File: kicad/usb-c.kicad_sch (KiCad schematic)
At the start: 12 parts, among them J201 USB_C_Receptacle_USB2.0_16P, Q201 NMOS, U201 TPD1S514-1YZR, U202 ESD122DMYR, U203 TPD2S300

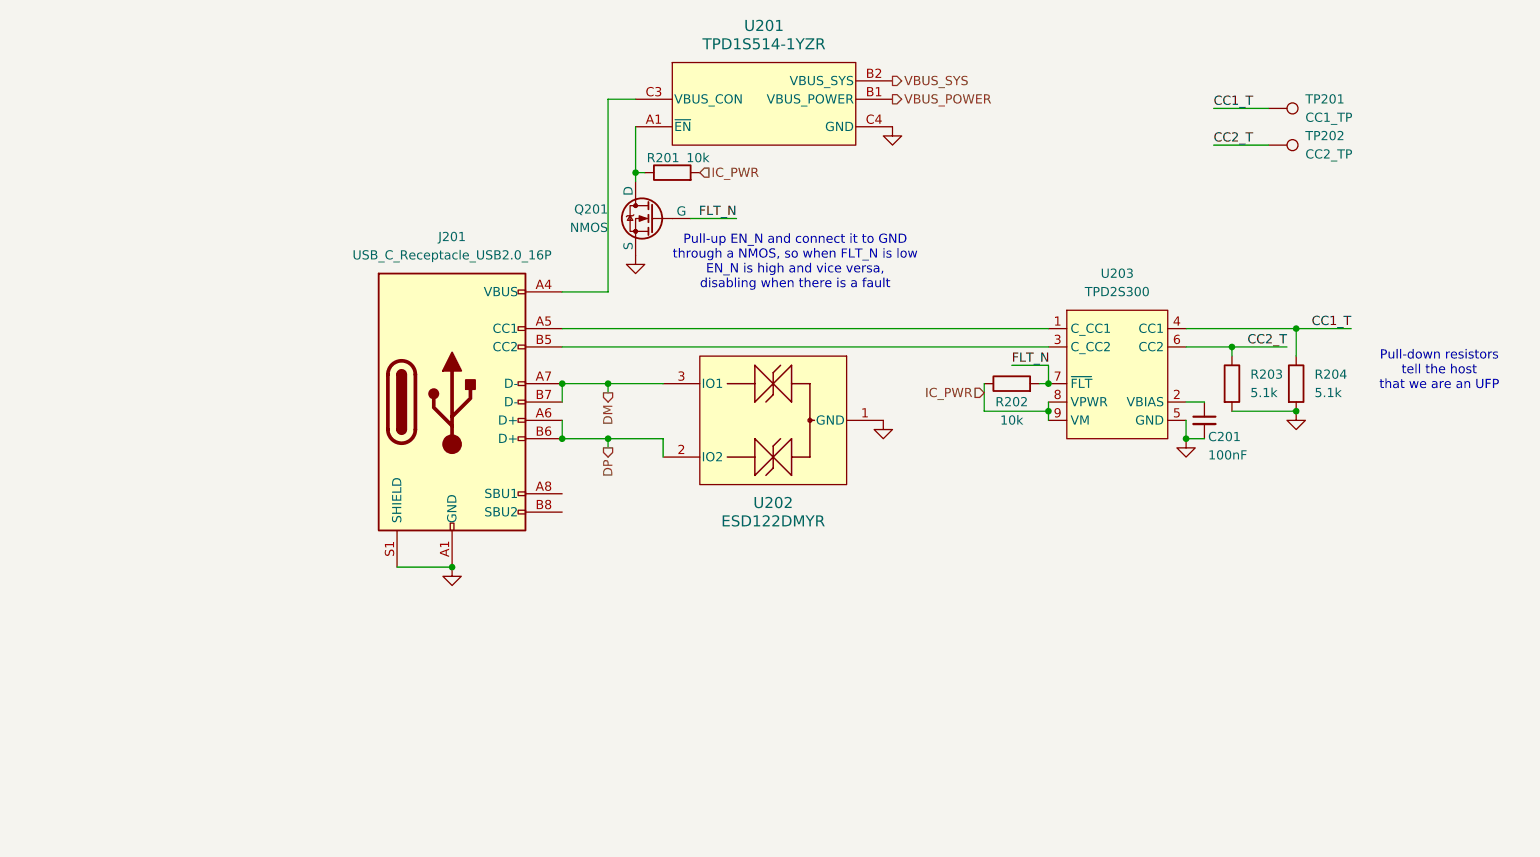
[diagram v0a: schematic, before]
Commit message: add datasheets, modularize current hardware
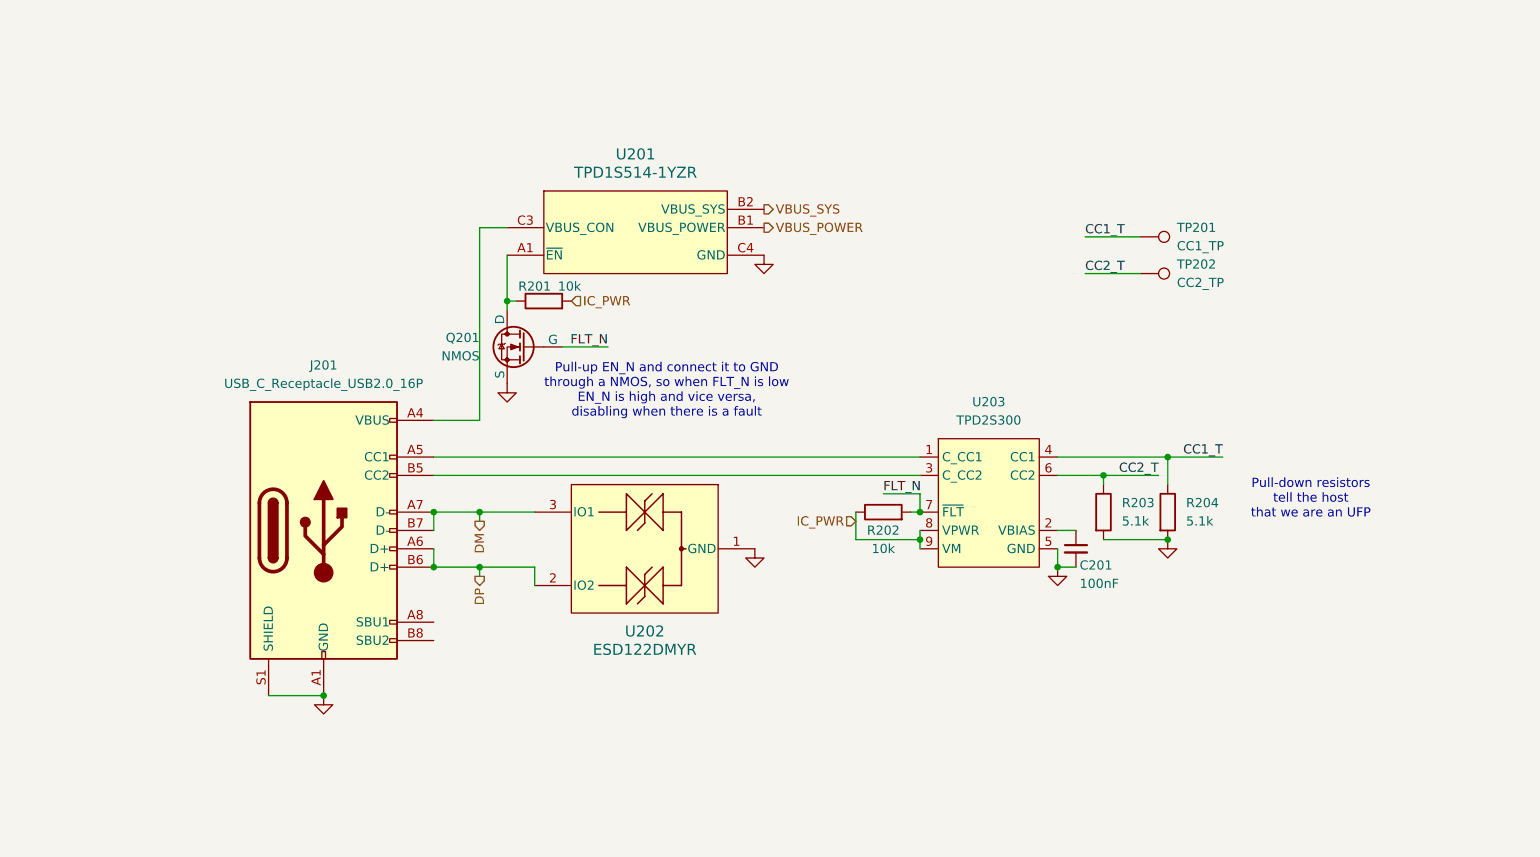
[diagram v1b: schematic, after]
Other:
- company: (none) -> Author: Lucas Merritt
- title: (none) -> USB-C Module
- moved on the sheet: C201, J201, Q201, R201, R202, R203, R204, TP201, TP202, U201, U202, U203

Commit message: add power v2, input, storage modules
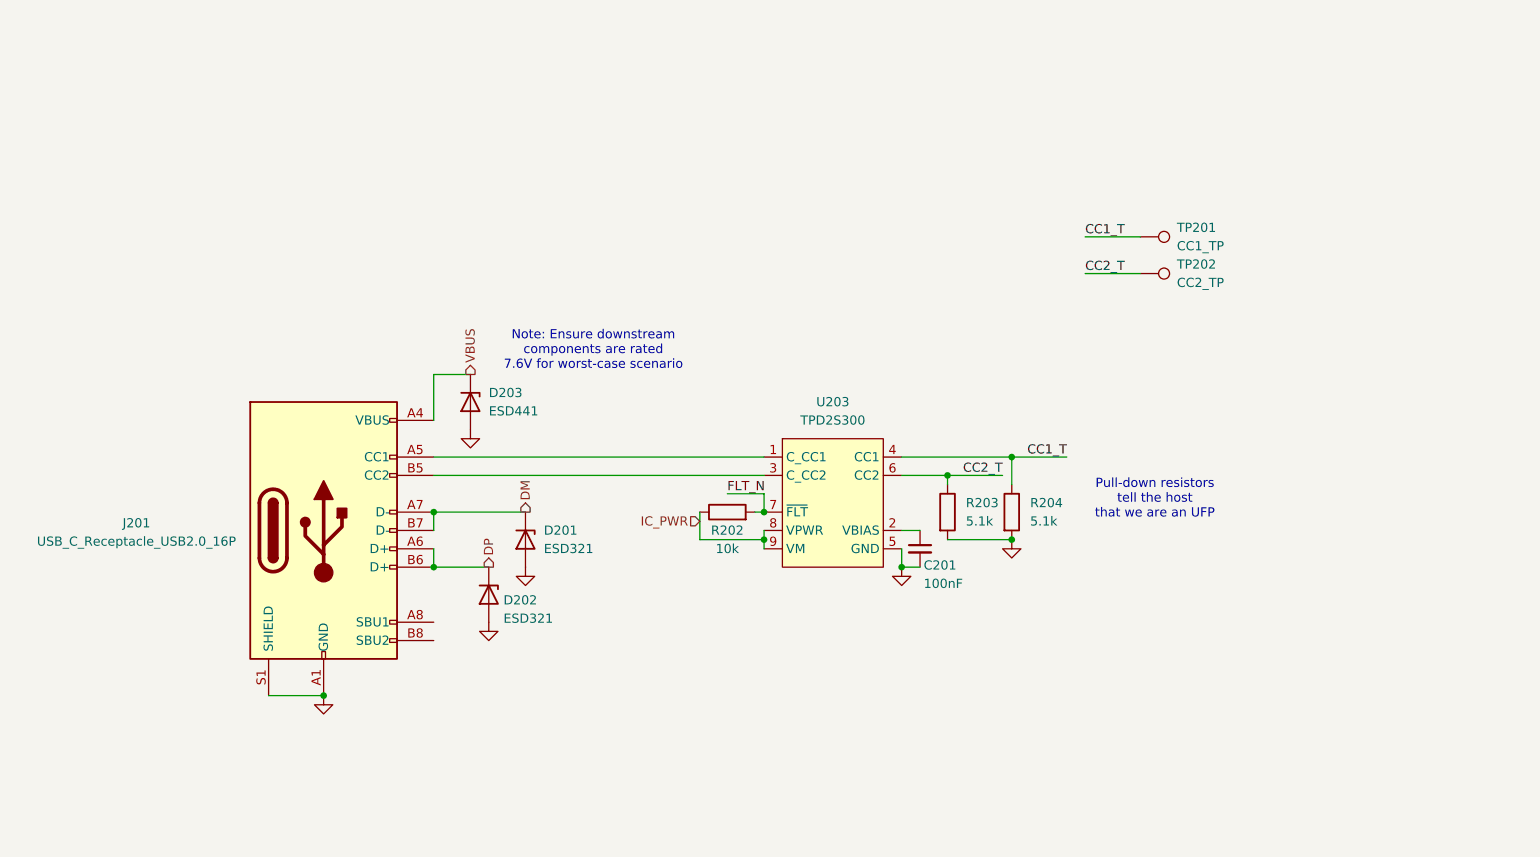
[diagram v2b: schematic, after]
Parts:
- removed Q201: NMOS, symbol Simulation_SPICE:NMOS
- removed R201: 10k, symbol Device:R
- removed U201: TPD1S514-1YZR, YZ0012-C01, symbol Raven:TPD1S514-1YZR
- removed U202: ESD122DMYR, DMY0003A, symbol Raven:ESD122DMYR
- added D201, D202: ESD321, symbol Device:D_Zener
- added D203: ESD441, symbol Device:D_Zener
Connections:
- net DM: now also D201.1 (K)
- net DP: now also D202.1 (K)
- net GND: now also D201.2 (A), D202.2 (A), D203.2 (A)
- net VBUS: now reaches J201.A4 (VBUS), J201.A9 (VBUS), J201.B4 (VBUS), J201.B9 (VBUS)
- net VBUS: now also D203.1 (K)
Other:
- note added: "Note: Ensure downstream components are rated 7.6V for worst-case scenario"
- note removed: "Pull-up EN_N and connect it to GND through a NMOS, so when FLT_N is low EN_N is high and vice versa, disabling when there is a fault"
- moved on the sheet: C201, R202, R203, R204, U203

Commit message: refactor, fix issues, ready for first design
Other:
- note added: "Note: Ensure downstream components are rated ~7.6V for worst-case scenario"
- note removed: "Note: Ensure downstream components are rated 7.6V for worst-case scenario"
- moved on the sheet: TP201, TP202
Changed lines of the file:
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@@
 		(rev "1")
 		(company "Author: Lucas Merritt")
-		(comment 1 "TODO: Consider dead-battery state operation")
 	)
 	(junction
@@
 	(wire
 		(pts
-			(xy 205.74 73.66) (xy 198.12 73.66)
+			(xy 144.78 149.86) (xy 137.16 149.86)
 		)
 		(stroke
@@
 	(wire
 		(pts
-			(xy 205.74 68.58) (xy 198.12 68.58)
+			(xy 144.78 144.78) (xy 137.16 144.78)
 		)
 		(stroke
@@
 		(pts
 			(xy 144.78 110.49) (xy 153.67 110.49)
-		)
-		(stroke
-			(width 0)
-			(type default)
-		)
-	)
-	(wire
-		(pts
-			(xy 148.59 104.14) (xy 153.67 104.14)
 		)
 		(stroke
@@
 		)
 	)
-	(text "Note: Ensure downstream\ncomponents are rated \n7.6V for worst-case scenario"
+	(text "Note: Ensure downstream\ncomponents are rated \n~7.6V for worst-case scenario"
 		(exclude_from_sim no)
 		(at 130.048 84.328 0)
@@
 	)
 	(label "CC2_T"
-		(at 198.12 73.66 0)
+		(at 137.16 149.86 0)
 		(fields_autoplaced yes)
 		(effects
@@
 	)
 	(label "CC1_T"
-		(at 198.12 68.58 0)
+		(at 137.16 144.78 0)
 		(fields_autoplaced yes)
 		(effects
@@
 		)
 	)
-	(label "FLT_N"
-		(at 148.59 104.14 0)
+	(hierarchical_label "DM"
+		(shape output)
+		(at 120.65 106.68 90)
 		(fields_autoplaced yes)
 		(effects
@@
 				(size 1.27 1.27)
 			)
-			(justify left bottom)
-		)
-	)
-	(hierarchical_label "DM"
-		(shape output)
-		(at 120.65 106.68 90)
+			(justify left)
+		)
+	)
+	(hierarchical_label "IC_PWR"
+		(shape input)
+		(at 144.78 107.95 180)
 		(fields_autoplaced yes)
 		(effects
@@
 				(size 1.27 1.27)
 			)
-			(justify left)
-		)
-	)
-	(hierarchical_label "IC_PWR"
-		(shape input)
-		(at 144.78 107.95 180)
+			(justify right)
+		)
+	)
+	(hierarchical_label "DP"
+		(shape output)
+		(at 115.57 114.3 90)
 		(fields_autoplaced yes)
 		(effects
@@
 				(size 1.27 1.27)
 			)
-			(justify right)
-		)
-	)
-	(hierarchical_label "DP"
+			(justify left)
+		)
+	)
+	(hierarchical_label "VBUS"
 		(shape output)
-		(at 115.57 114.3 90)
+		(at 113.03 87.63 90)
 		(fields_autoplaced yes)
 		(effects
@@
 		)
 	)
-	(hierarchical_label "VBUS"
+	(hierarchical_label "FLT_N"
 		(shape output)
-		(at 113.03 87.63 90)
+		(at 153.67 104.14 180)
 		(fields_autoplaced yes)
 		(effects
@@
 				(size 1.27 1.27)
 			)
-			(justify left)
+			(justify right)
 		)
 	)
@@
 		(on_board yes)
 		(dnp no)
-		(fields_autoplaced yes)
 		(property "Reference" "R203"
-			(at 181.61 105.4099 0)
+			(at 180.848 105.41 0)
 			(effects
 				(font
@@
 		)
 		(property "Value" "5.1k"
-			(at 181.61 107.9499 0)
+			(at 180.848 107.95 0)
 			(effects
 				(font
@@
 	(symbol
 		(lib_id "Connector:TestPoint")
-		(at 205.74 73.66 270)
+		(at 144.78 149.86 270)
 		(unit 1)
 		(exclude_from_sim no)
@@
 		(fields_autoplaced yes)
 		(property "Reference" "TP202"
-			(at 210.82 72.3899 90)
+			(at 149.86 148.5899 90)
 			(effects
 				(font
@@
 		)
 		(property "Value" "CC2_TP"
-			(at 210.82 74.9299 90)
+			(at 149.86 151.1299 90)
 			(effects
 				(font
@@
 		)
 		(property "Footprint" ""
-			(at 205.74 78.74 0)
+			(at 144.78 154.94 0)
 			(effects
 				(font
@@
 		)
 		(property "Datasheet" "~"
-			(at 205.74 78.74 0)
+			(at 144.78 154.94 0)
 			(effects
 				(font
@@
 		)
 		(property "Description" "test point"
-			(at 205.74 73.66 0)
+			(at 144.78 149.86 0)
 			(effects
 				(font
@@
 	(symbol
 		(lib_id "Connector:TestPoint")
-		(at 205.74 68.58 270)
+		(at 144.78 144.78 270)
 		(unit 1)
 		(exclude_from_sim no)
@@
 		(fields_autoplaced yes)
 		(property "Reference" "TP201"
-			(at 210.82 67.3099 90)
+			(at 149.86 143.5099 90)
 			(effects
 				(font
@@
 		)
 		(property "Value" "CC1_TP"
-			(at 210.82 69.8499 90)
+			(at 149.86 146.0499 90)
 			(effects
 				(font
@@
 		)
 		(property "Footprint" ""
-			(at 205.74 73.66 0)
+			(at 144.78 149.86 0)
 			(effects
 				(font
@@
 		)
 		(property "Datasheet" "~"
-			(at 205.74 73.66 0)
+			(at 144.78 149.86 0)
 			(effects
 				(font
@@
 		)
 		(property "Description" "test point"
-			(at 205.74 68.58 0)
-			(effects
-				(font
+			(at 144.78 144.78 0)
+			(effects
+				(font

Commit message: essentially finish schematic, start adding footprints, add new footprints
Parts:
- C201: footprint (none) -> Capacitor_SMD:C_0603_1608Metric_Pad1.08x0.95mm_HandSolder
- D201: renamed from D203; value ESD441 -> TPD1E05U06-Q1; footprint (none) -> Package_SON:Texas_DPY0002A_0.6x1mm_P0.65mm
- D202: footprint (none) -> Diode_SMD:D_SOD-523
- D203: renamed from D201; footprint (none) -> Diode_SMD:D_SOD-523
- J201: footprint (none) -> Raven:GCT_USB4105-GF-A-16P
- R201: renamed from R202; footprint (none) -> Resistor_SMD:R_0603_1608Metric_Pad0.98x0.95mm_HandSolder
- R202: renamed from R203; footprint (none) -> Resistor_SMD:R_0603_1608Metric_Pad0.98x0.95mm_HandSolder
- R203: renamed from R204; footprint (none) -> Resistor_SMD:R_0603_1608Metric_Pad0.98x0.95mm_HandSolder
- TP201, TP202: footprint (none) -> TestPoint:TestPoint_Pad_D3.0mm
- U201: renamed from U203; footprint YFF0009AJAJ -> Raven:YFF0009AJAJ
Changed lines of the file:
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@@
 			)
 		)
-		(property "Footprint" ""
+		(property "Footprint" "Capacitor_SMD:C_0603_1608Metric_Pad1.08x0.95mm_HandSolder"
 			(at 175.26 111.76 0)
 			(effects
@@
 		(dnp no)
 		(fields_autoplaced yes)
-		(property "Reference" "D203"
+		(property "Reference" "D201"
 			(at 115.57 90.1699 90)
 			(effects
@@
 			)
 		)
-		(property "Value" "ESD441"
+		(property "Value" "TPD1E05U06-Q1"
 			(at 115.57 92.7099 90)
 			(effects
@@
 			)
 		)
-		(property "Footprint" ""
+		(property "Footprint" "Package_SON:Texas_DPY0002A_0.6x1mm_P0.65mm"
 			(at 113.03 91.44 0)
 			(effects
@@
 			(project "kicad"
 				(path "/97e37379-fec6-4f0d-82d9-4ea53516bb02/32d68f15-4a24-4df9-a303-ad9032613b76"
-					(reference "D203")
+					(reference "D201")
 					(unit 1)
 				)
@@
 		(on_board yes)
 		(dnp no)
-		(property "Reference" "R202"
+		(property "Reference" "R201"
 			(at 148.59 109.22 90)
 			(effects
@@
 			)
 		)
-		(property "Footprint" ""
+		(property "Footprint" "Resistor_SMD:R_0603_1608Metric_Pad0.98x0.95mm_HandSolder"
 			(at 148.59 108.458 90)
 			(effects
@@
 			(project "kicad"
 				(path "/97e37379-fec6-4f0d-82d9-4ea53516bb02/32d68f15-4a24-4df9-a303-ad9032613b76"
-					(reference "R202")
+					(reference "R201")
 					(unit 1)
 				)
@@
 		(on_board yes)
 		(dnp no)
-		(property "Reference" "R203"
+		(property "Reference" "R202"
 			(at 180.848 105.41 0)
 			(effects
@@
 			)
 		)
-		(property "Footprint" ""
+		(property "Footprint" "Resistor_SMD:R_0603_1608Metric_Pad0.98x0.95mm_HandSolder"
 			(at 177.292 106.68 90)
 			(effects
@@
 			(project "kicad"
 				(path "/97e37379-fec6-4f0d-82d9-4ea53516bb02/32d68f15-4a24-4df9-a303-ad9032613b76"
-					(reference "R203")
+					(reference "R202")
 					(unit 1)
 				)
@@
 		(dnp no)
 		(fields_autoplaced yes)
-		(property "Reference" "#PWR0203"
+		(property "Reference" "#PWR0204"
 			(at 120.65 120.65 0)
 			(effects
@@
 			(project "kicad"
 				(path "/97e37379-fec6-4f0d-82d9-4ea53516bb02/32d68f15-4a24-4df9-a303-ad9032613b76"
-					(reference "#PWR0203")
+					(reference "#PWR0204")
 					(unit 1)
 				)
@@
 		(dnp no)
 		(fields_autoplaced yes)
-		(property "Reference" "R204"
+		(property "Reference" "R203"
 			(at 190.5 105.4099 0)
 			(effects
@@
 			)
 		)
-		(property "Footprint" ""
+		(property "Footprint" "Resistor_SMD:R_0603_1608Metric_Pad0.98x0.95mm_HandSolder"
 			(at 186.182 106.68 90)
 			(effects
@@
 			(project "kicad"
 				(path "/97e37379-fec6-4f0d-82d9-4ea53516bb02/32d68f15-4a24-4df9-a303-ad9032613b76"
-					(reference "R204")
+					(reference "R203")
 					(unit 1)
 				)
@@
 			)
 		)
-		(property "Footprint" ""
+		(property "Footprint" "TestPoint:TestPoint_Pad_D3.0mm"
 			(at 144.78 154.94 0)
 			(effects
@@
 		(dnp no)
 		(fields_autoplaced yes)
-		(property "Reference" "U203"
+		(property "Reference" "U201"
 			(at 163.195 91.44 0)
 			(effects
@@
 			)
 		)
-		(property "Footprint" "YFF0009AJAJ"
+		(property "Footprint" "Raven:YFF0009AJAJ"
 			(at 167.64 115.57 0)
 			(effects
@@
 			(project "kicad"
 				(path "/97e37379-fec6-4f0d-82d9-4ea53516bb02/32d68f15-4a24-4df9-a303-ad9032613b76"
-					(reference "U203")
+					(reference "U201")
 					(unit 1)
 				)
@@
 		(dnp no)
 		(fields_autoplaced yes)
-		(property "Reference" "D201"
+		(property "Reference" "D203"
 			(at 123.19 109.2199 90)
 			(effects
@@
 			)
 		)
-		(property "Footprint" ""
+		(property "Footprint" "Diode_SMD:D_SOD-523"
 			(at 120.65 110.49 0)
 			(effects
@@
 			(project "kicad"
 				(path "/97e37379-fec6-4f0d-82d9-4ea53516bb02/32d68f15-4a24-4df9-a303-ad9032613b76"
-					(reference "D201")
+					(reference "D203")
 					(unit 1)
 				)
@@
 			)
 		)
-		(property "Footprint" ""
+		(property "Footprint" "TestPoint:TestPoint_Pad_D3.0mm"
 			(at 144.78 149.86 0)
 			(effects
@@
 			)
 		)
-		(property "Footprint" ""
+		(property "Footprint" "Diode_SMD:D_SOD-523"
 			(at 115.57 118.11 0)
 			(effects
@@
 		(dnp no)
 		(fields_autoplaced yes)
-		(property "Reference" "#PWR0207"
+		(property "Reference" "#PWR0203"
 			(at 115.57 128.27 0)
 			(effects
@@
 			(project "kicad"
 				(path "/97e37379-fec6-4f0d-82d9-4ea53516bb02/32d68f15-4a24-4df9-a303-ad9032613b76"
-					(reference "#PWR0207")
+					(reference "#PWR0203")
 					(unit 1)
 				)
@@
 			)
 		)
-		(property "Footprint" ""
+		(property "Footprint" "Raven:GCT_USB4105-GF-A-16P"
 			(at 96.52 109.22 0)
 			(effects

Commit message: fix motor with spring fingers, start PCB
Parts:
- TP201, TP202: footprint TestPoint:TestPoint_Pad_D3.0mm -> TestPoint:TestPoint_Pad_D1.5mm
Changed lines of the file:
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@@
 			)
 		)
-		(property "Footprint" "TestPoint:TestPoint_Pad_D3.0mm"
+		(property "Footprint" "TestPoint:TestPoint_Pad_D1.5mm"
 			(at 144.78 154.94 0)
 			(effects
@@
 			)
 		)
-		(property "Footprint" "TestPoint:TestPoint_Pad_D3.0mm"
+		(property "Footprint" "TestPoint:TestPoint_Pad_D1.5mm"
 			(at 144.78 149.86 0)
 			(effects

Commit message: finish PCB routing, need silkscreen + checks
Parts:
- added C203: 1uF, Capacitor_SMD:C_0805_2012Metric_Pad1.18x1.45mm_HandSolder, symbol Device:C
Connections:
- net GND: now also C203.2
- net IC_PWR: now also C203.1
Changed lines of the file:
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@@
+	)
+	(junction
+		(at 144.78 110.49)
+		(diameter 0)
+		(color 0 0 0 0)
 	)
 	(junction
@@
 	)
 	(symbol
+		(lib_id "Device:C")
+		(at 144.78 114.3 0)
+		(unit 1)
+		(exclude_from_sim no)
+		(in_bom yes)
+		(on_board yes)
+		(dnp no)
+		(property "Reference" "C203"
+			(at 147.828 114.046 0)
+			(effects
+				(font
+					(size 1.27 1.27)
+				)
+				(justify left)
+			)
+		)
+		(property "Value" "1uF"
+			(at 147.828 116.586 0)
+			(effects
+				(font
+					(size 1.27 1.27)
+				)
+				(justify left)
+			)
+		)
+		(property "Footprint" "Capacitor_SMD:C_0805_2012Metric_Pad1.18x1.45mm_HandSolder"
+			(at 145.7452 118.11 0)
+			(effects
+				(font
+					(size 1.27 1.27)
+				)
+				(hide yes)
+			)
+		)
+		(property "Datasheet" "~"
+			(at 144.78 114.3 0)
+			(effects
+				(font
+					(size 1.27 1.27)
+				)
+				(hide yes)
+			)
+		)
+		(property "Description" "Unpolarized capacitor"
+			(at 144.78 114.3 0)
+			(effects
+				(font
+					(size 1.27 1.27)
+				)
+				(hide yes)
+			)
+		)
+		(pin "2"
+		)
+		(pin "1"
+		)
+		(instances
+			(project "kicad"
+				(path "/97e37379-fec6-4f0d-82d9-4ea53516bb02/32d68f15-4a24-4df9-a303-ad9032613b76"
+					(reference "C203")
+					(unit 1)
+				)
+			)
+		)
+	)
+	(symbol
 		(lib_id "power:GND")
 		(at 120.65 114.3 0)
@@
 					(unit 1)
 				)
+			)
+		)
+	)
+	(symbol
+		(lib_id "power:GND")
+		(at 144.78 118.11 0)
+		(unit 1)
+		(exclude_from_sim no)
+		(in_bom yes)
+		(on_board yes)
+		(dnp no)
+		(fields_autoplaced yes)
+		(property "Reference" "#PWR0207"
+			(at 144.78 124.46 0)
+			(effects
+				(font
+					(size 1.27 1.27)
+				)
+				(hide yes)
+			)
+		)
+		(property "Value" "GND"
+			(at 144.78 123.19 0)
+			(effects
+				(font
+					(size 1.27 1.27)
+				)
+				(hide yes)
+			)
+		)
+		(property "Footprint" ""
+			(at 144.78 118.11 0)
+			(effects
+				(font
+					(size 1.27 1.27)
+				)
+				(hide yes)
+			)
+		)
+		(property "Datasheet" ""
+			(at 144.78 118.11 0)
+			(effects
+				(font
+					(size 1.27 1.27)
+				)
+				(hide yes)
+			)
+		)
+		(property "Description" "Power symbol creates a global label with name \"GND\" , ground"
+			(at 144.78 118.11 0)
+			(effects
+				(font
+					(size 1.27 1.27)
+				)
+				(hide yes)
+			)
+		)
+		(pin "1"
+		)
+		(instances
+			(project "kicad"
+				(path "/97e37379-fec6-4f0d-82d9-4ea53516bb02/32d68f15-4a24-4df9-a303-ad9032613b76"
+					(reference "#PWR0207")
+					(unit 1)
+				)
